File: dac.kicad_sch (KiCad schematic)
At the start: 1 part, among them U16 DAC80504

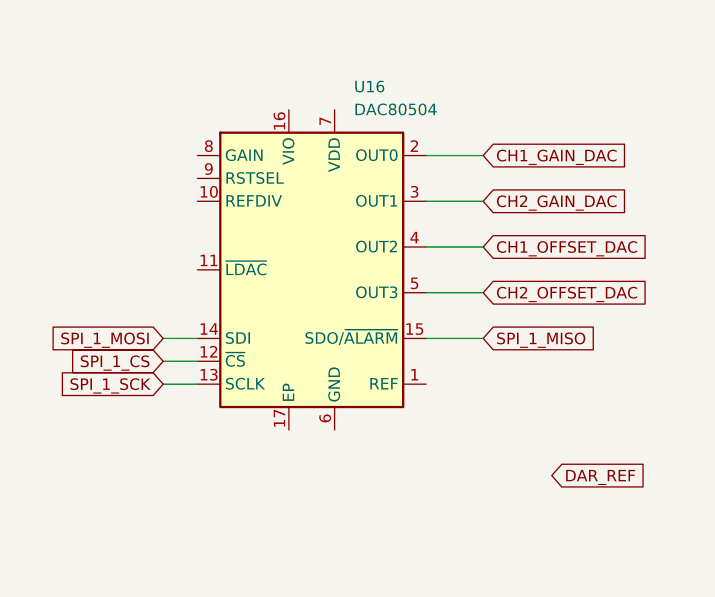
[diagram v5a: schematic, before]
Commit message: Simplifying the design
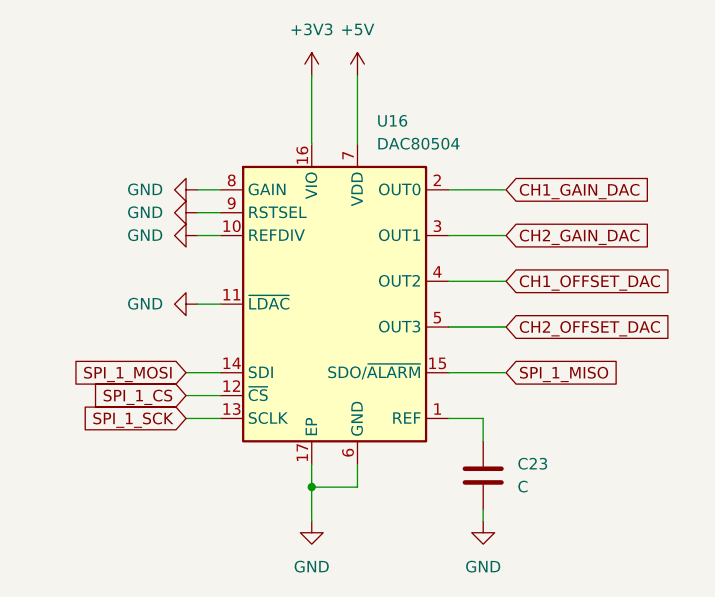
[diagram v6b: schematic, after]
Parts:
- added C23: C, symbol Device:C
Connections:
- net at U16.1 (REF): now also C23.1
- net GND: now reaches U16.10 (REFDIV)
- net GND: now also U16.11 (~{LDAC}), U16.17 (EP), U16.6 (GND), U16.8 (GAIN), U16.9 (RSTSEL), C23.2
- net +3V3: now reaches U16.16 (VIO)
- net +5V: now reaches U16.7 (VDD)
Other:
- moved on the sheet: U16

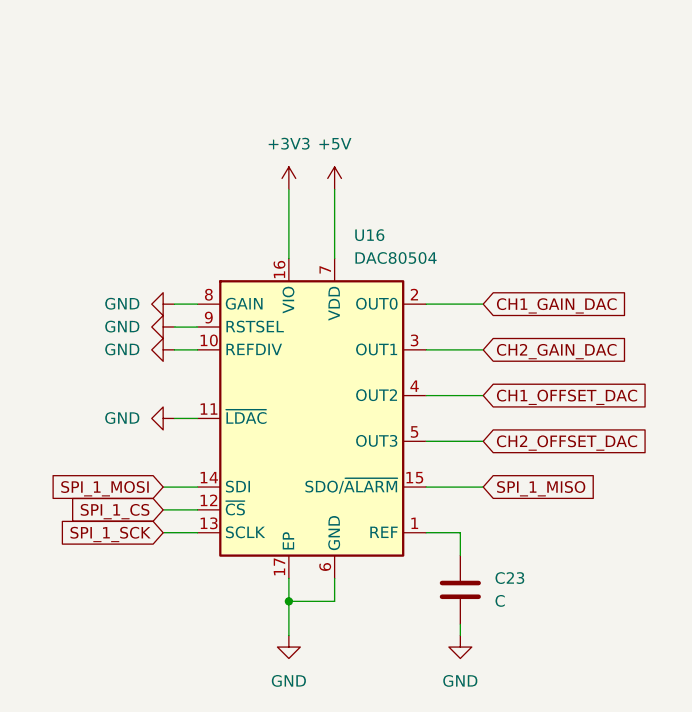
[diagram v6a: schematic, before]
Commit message: Mostly finished schematics, without decoupling and power
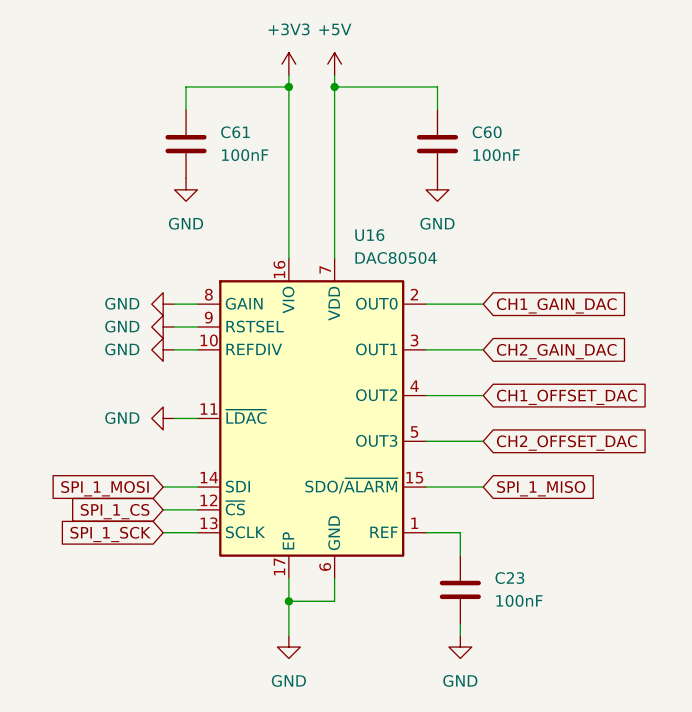
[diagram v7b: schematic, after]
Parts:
- added C60, C61: 100nF, symbol Device:C
- C23: value C -> 100nF
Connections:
- net +3V3: now also C61.1
- net +5V: now also C60.1
- net GND: now also C60.2, C61.2

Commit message: Finished schematic?
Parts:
- added C26, C29: 0.1uF, symbol Device:C
- added C28, C30: 1uF, symbol Device:C
- C60, C61: value 100nF -> 100pF
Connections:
- net +3V3: now also C29.1, C30.1
- net +5V: now also C26.1, C28.1
- net GND: now also C26.2, C28.2, C29.2, C30.2
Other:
- moved on the sheet: C23, C60, C61, U16
